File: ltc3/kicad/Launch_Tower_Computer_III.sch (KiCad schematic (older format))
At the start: 0 parts

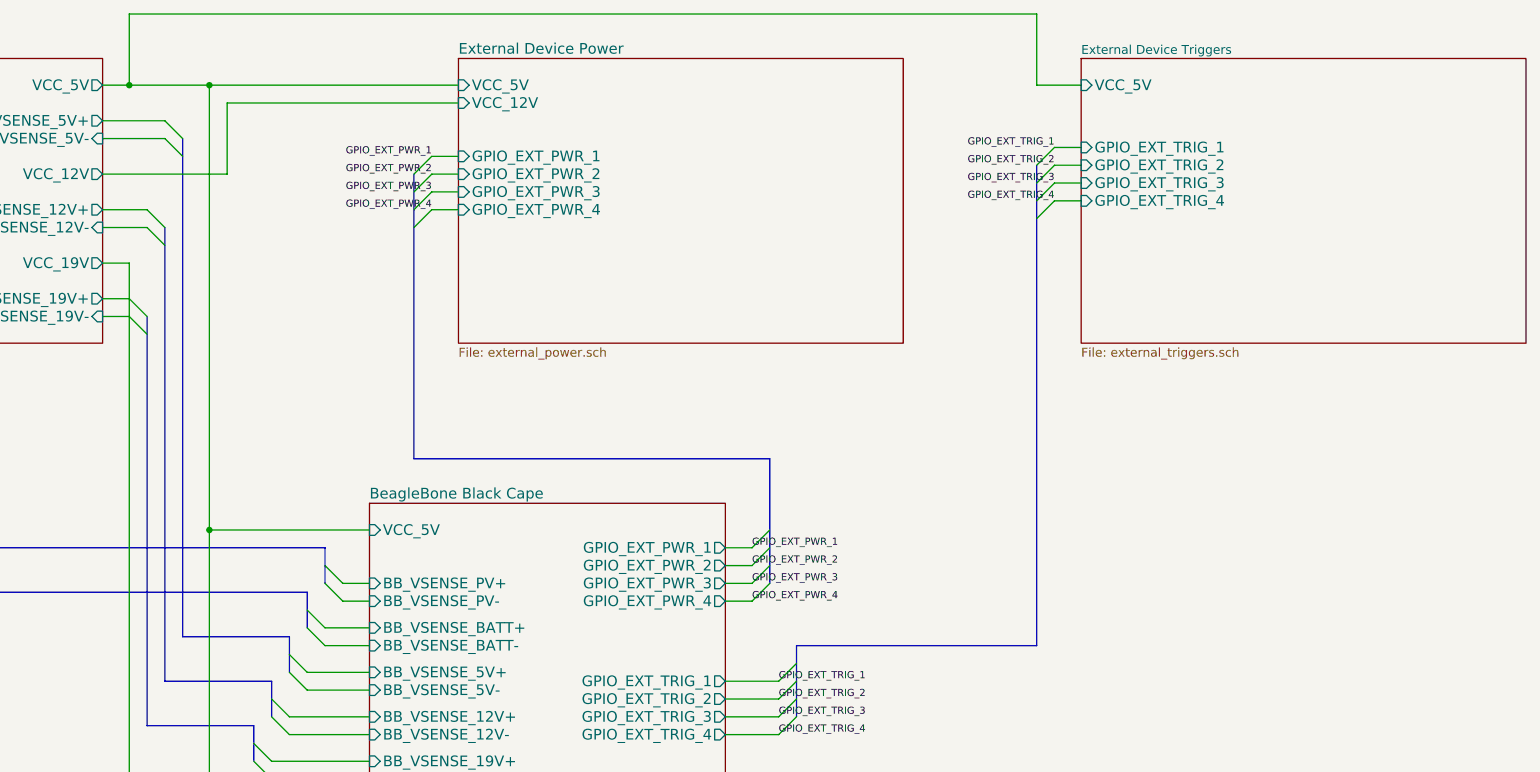
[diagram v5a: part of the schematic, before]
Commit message: Combined external power and trigger sheets.
Still need to make the page pretty.
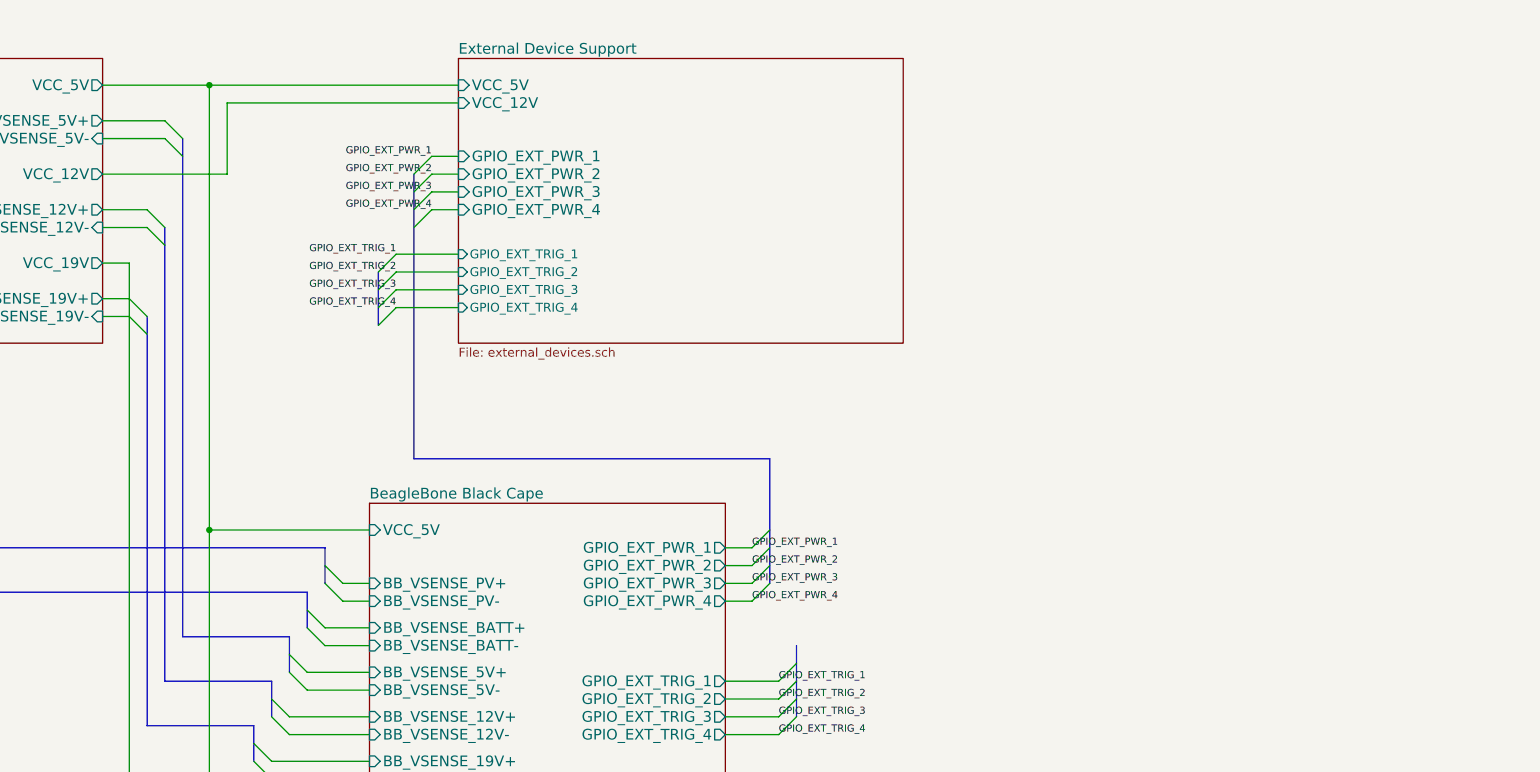
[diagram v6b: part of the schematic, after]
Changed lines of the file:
@@
 $Descr B 17000 11000
 encoding utf-8
-Sheet 1 8
+Sheet 1 7
 Title "Launch Tower Computer 3 (LTC3)"
 Date "2015-11-20"
@@
 	9400 2350 9500 2250
 Entry Wire Line
-	12900 2000 13000 1900
-Entry Wire Line
-	12900 2100 13000 2000
-Entry Wire Line
-	12900 2200 13000 2100
-Entry Wire Line
-	12900 2300 13000 2200
+	9200 2600 9300 2500
+Entry Wire Line
+	9200 2700 9300 2600
+Entry Wire Line
+	9200 2800 9300 2700
+Entry Wire Line
+	9200 2900 9300 2800
 Text Label 11300 4150 0    40   ~ 0
 GPIO_EXT_PWR_1
@@
 Text Label 9500 2250 2    40   ~ 0
 GPIO_EXT_PWR_4
-Text Label 13000 1900 2    40   ~ 0
+Text Label 9300 2500 2    40   ~ 0
 GPIO_EXT_TRIG_1
-Text Label 13000 2000 2    40   ~ 0
+Text Label 9300 2600 2    40   ~ 0
 GPIO_EXT_TRIG_2
-Text Label 13000 2100 2    40   ~ 0
+Text Label 9300 2700 2    40   ~ 0
 GPIO_EXT_TRIG_3
-Text Label 13000 2200 2    40   ~ 0
+Text Label 9300 2800 2    40   ~ 0
 GPIO_EXT_TRIG_4
 $Sheet
@@
 S 9650 1400 2500 1600
 U 551C79BE
-F0 "External Device Power" 60
-F1 "external_power.sch" 50
+F0 "External Device Support" 60
+F1 "external_devices.sch" 50
 F2 "VCC_12V" I L 9650 1650 60
 F3 "VCC_5V" I L 9650 1550 60
@@
 F6 "GPIO_EXT_PWR_4" I L 9650 2250 60
 F7 "GPIO_EXT_PWR_3" I L 9650 2150 60
-$EndSheet
-$Sheet
-S 13150 1400 2500 1600
-U 553268FD
-F0 "External Device Triggers" 50
-F1 "external_triggers.sch" 50
-F2 "GPIO_EXT_TRIG_1" I L 13150 1900 60
-F3 "VCC_5V" I L 13150 1550 60
-F4 "GPIO_EXT_TRIG_2" I L 13150 2000 60
-F5 "GPIO_EXT_TRIG_3" I L 13150 2100 60
-F6 "GPIO_EXT_TRIG_4" I L 13150 2200 60
+F8 "GPIO_EXT_TRIG_1" I L 9650 2500 50
+F9 "GPIO_EXT_TRIG_2" I L 9650 2600 50
+F10 "GPIO_EXT_TRIG_3" I L 9650 2700 50
+F11 "GPIO_EXT_TRIG_4" I L 9650 2800 50
 $EndSheet
 Text Notes 12300 9200 0    100  ~ 0
@@
 	9650 2250 9500 2250
 Wire Wire Line
-	13150 1900 13000 1900
-Wire Wire Line
-	13150 2000 13000 2000
-Wire Wire Line
-	13150 2100 13000 2100
-Wire Wire Line
-	13150 2200 13000 2200
+	9650 2500 9300 2500
+Wire Wire Line
+	9650 2600 9300 2600
+Wire Wire Line
+	9650 2700 9300 2700
+Wire Wire Line
+	9650 2800 9300 2800
 Wire Wire Line
 	7650 1550 9650 1550
@@
 Wire Bus Line
 	9400 2050 9400 3650
-Wire Bus Line
-	12900 2000 12900 4700
-Wire Bus Line
-	12900 4700 11550 4700
 Wire Bus Line
 	11550 4700 11550 5100
@@
 	8350 1650 9650 1650
 Wire Wire Line
-	7800 1550 7800 1150
-Wire Wire Line
-	7800 1150 12900 1150
-Wire Wire Line
-	12900 1150 12900 1550
-Wire Wire Line
-	12900 1550 13150 1550
-Connection ~ 7800 1550
-Wire Wire Line
 	9150 5600 4900 5600
 Wire Wire Line
@@
 Wire Wire Line
 	4900 5600 4900 1750
+Wire Bus Line
+	9200 2600 9200 2900
 $EndSCHEMATC

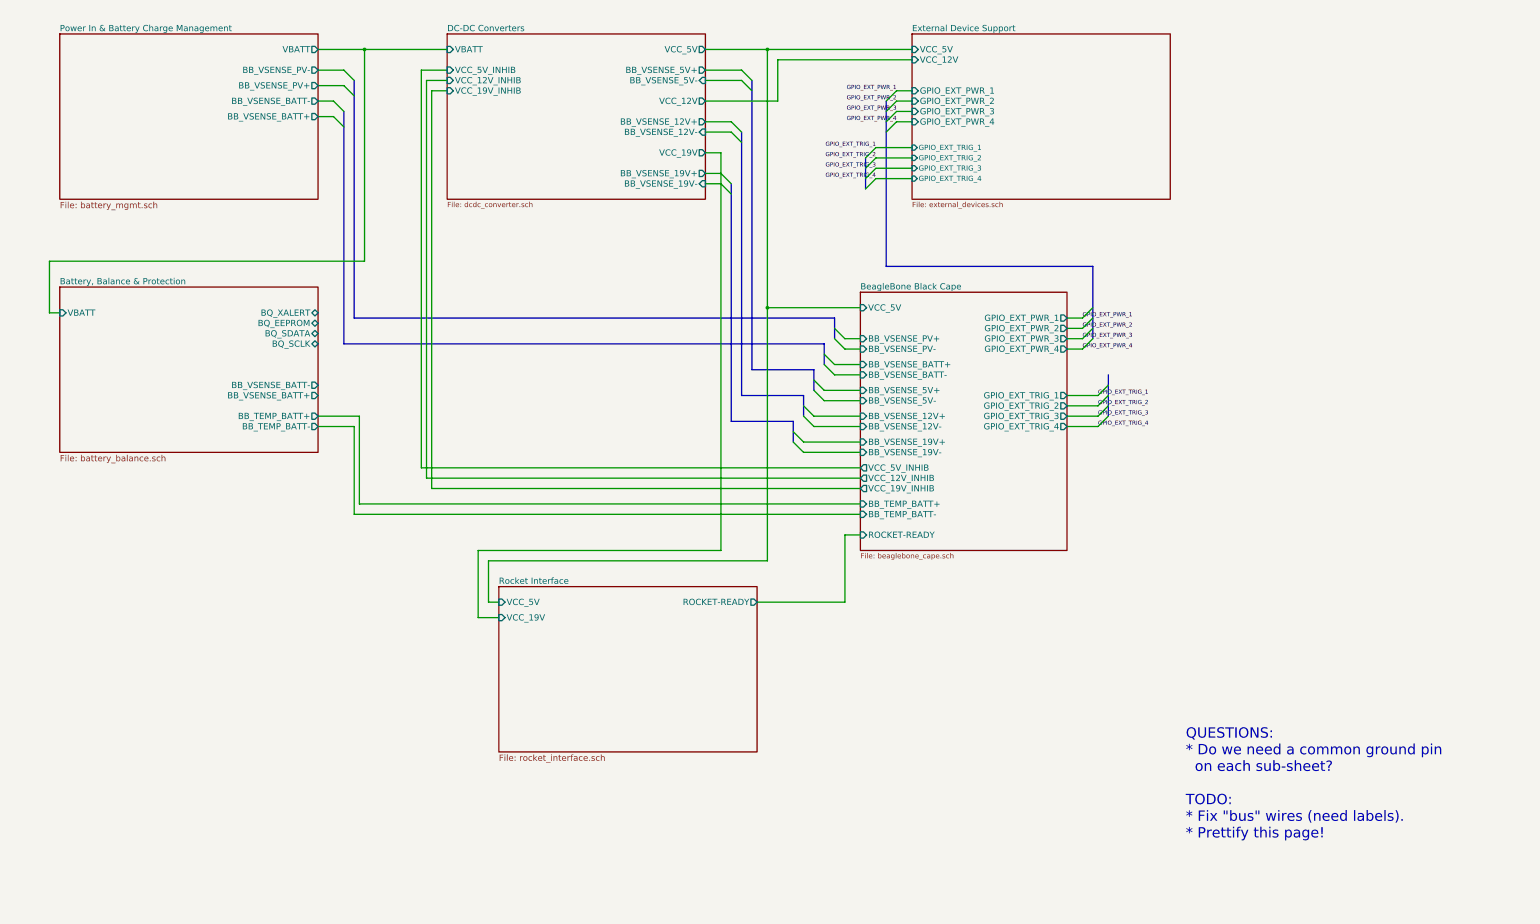
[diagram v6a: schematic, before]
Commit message: LTC3: Converted hierarchical power pins to global power nodes.
This eliminates the need to manually route power from one top-level
sheet to another.
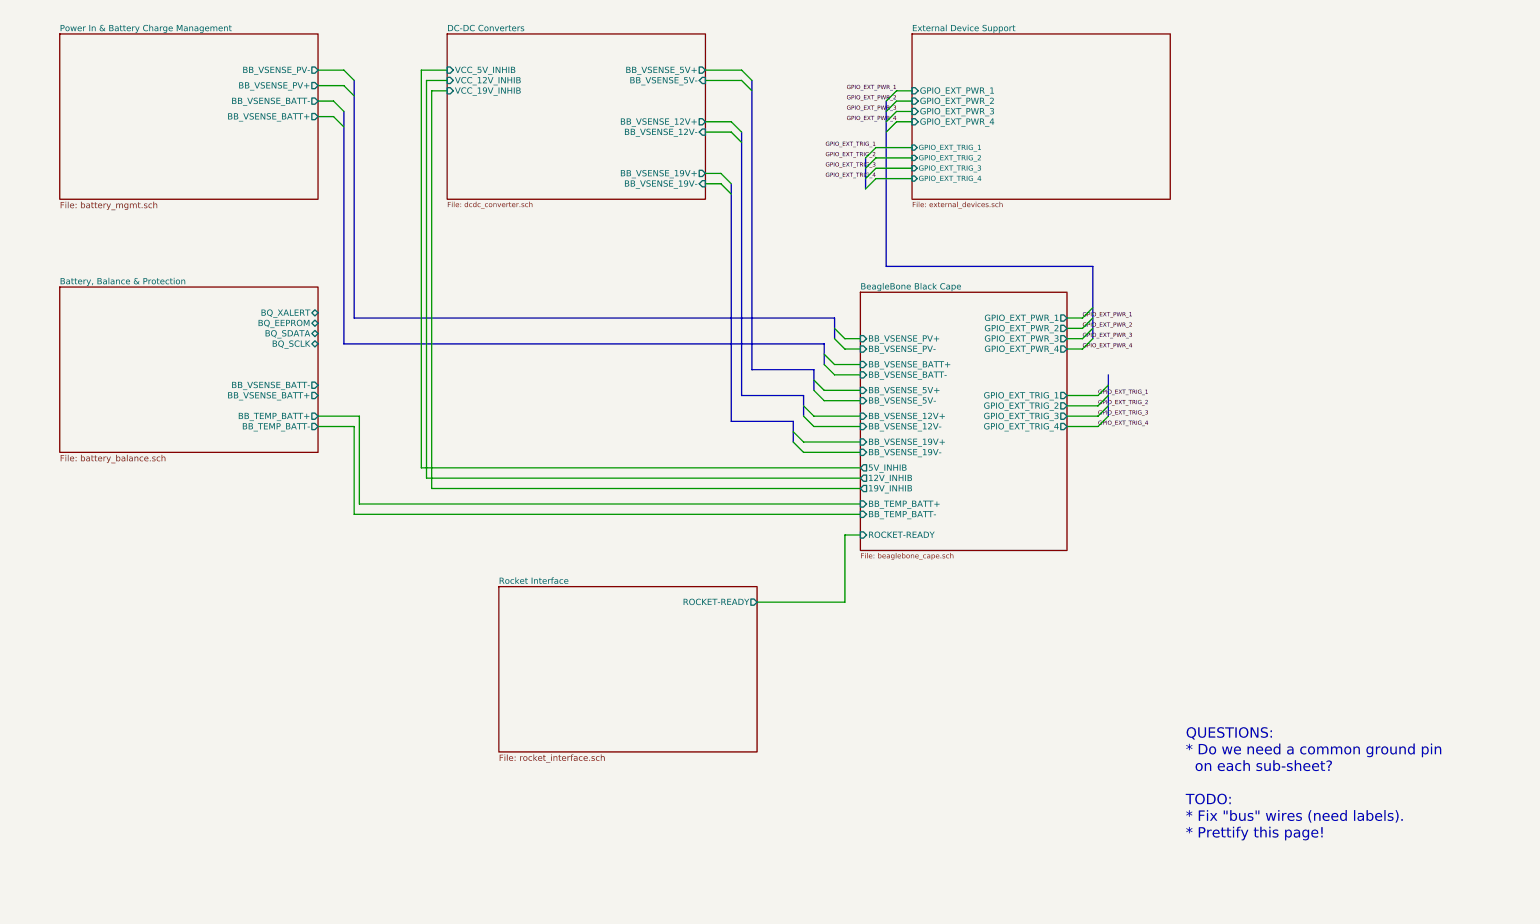
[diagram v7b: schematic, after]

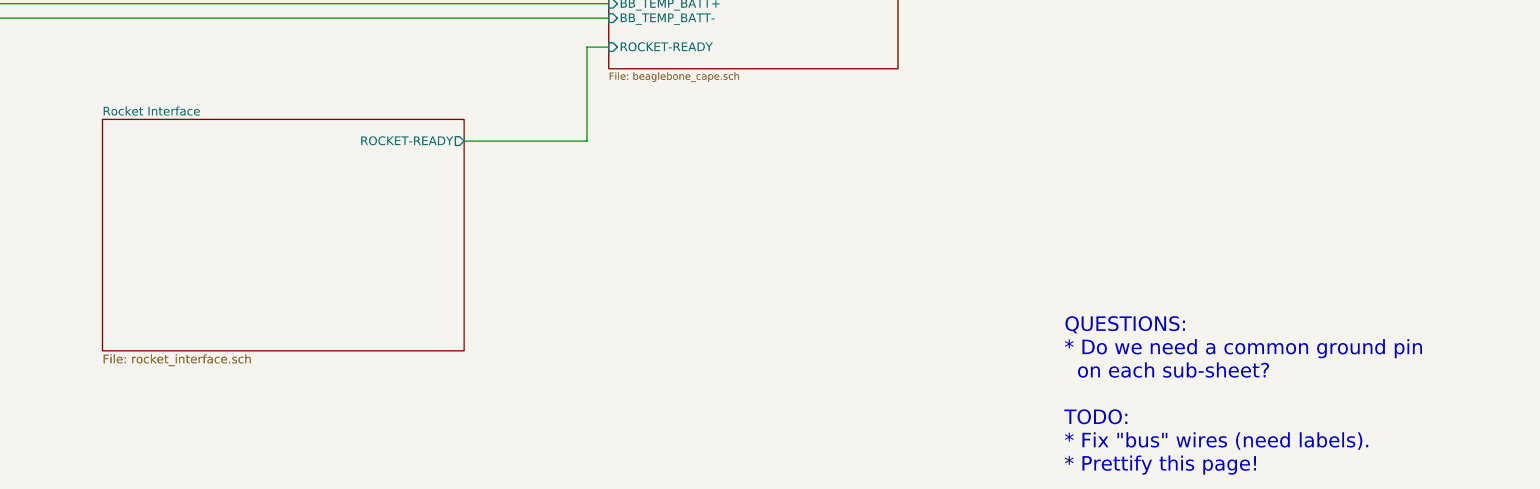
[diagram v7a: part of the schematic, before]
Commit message: LTC3: Misc. edits to rocket umbilical schematic.
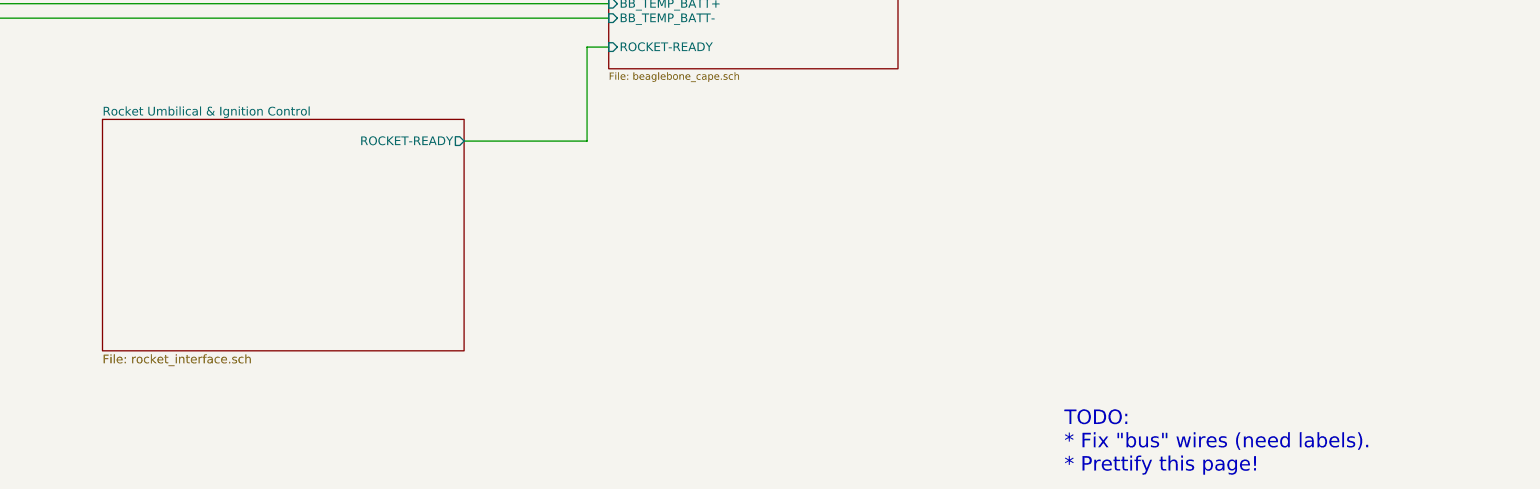
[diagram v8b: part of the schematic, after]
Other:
- note added: "TODO:\n* Fix "bus" wires (need labels).\n* Prettify this page!"
- note removed: "QUESTIONS:\n* Do we need a common ground pin\n on each sub-sheet?\n\nTODO:\n* Fix "bus" wires (need labels).\n* Prettify this page!"
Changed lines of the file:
@@
 LIBS:CD74HC14
 LIBS:power_nodes
+LIBS:relay_1c
 LIBS:Launch_Tower_Computer_III-cache
 EELAYER 25 0
@@
 S 5650 6750 2500 1600
 U 5598112B
-F0 "Rocket Interface" 60
+F0 "Rocket Umbilical & Ignition Control" 60
 F1 "rocket_interface.sch" 60
 F2 "ROCKET-READY" O R 8150 6900 60
@@
 $EndSheet
 Text Notes 12300 9200 0    100  ~ 0
-QUESTIONS:\n* Do we need a common ground pin\n  on each sub-sheet?\n\nTODO:\n* Fix "bus" wires (need labels).\n* Prettify this page!
+TODO:\n* Fix "bus" wires (need labels).\n* Prettify this page!
 Entry Wire Line
 	8000 1750 8100 1850
